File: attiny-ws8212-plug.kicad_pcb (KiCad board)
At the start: 2 copper layers, 25.4 x 22.9 mm, 5 parts, among them J1 USB_A, J2 WS2812, J3 WS2812, J4 WS2812, U1 ATtiny13-20PU

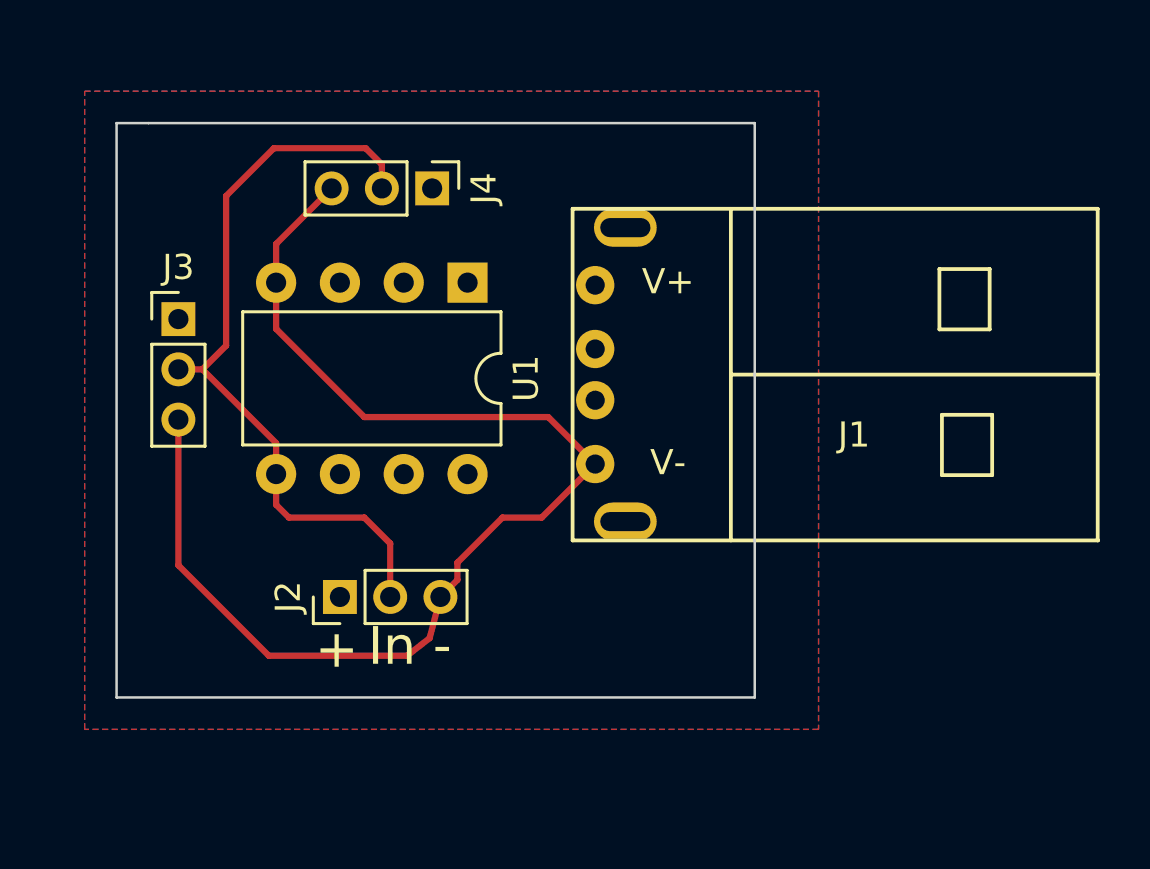
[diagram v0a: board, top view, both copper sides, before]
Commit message: Update schematics to 2.54mm of the pins
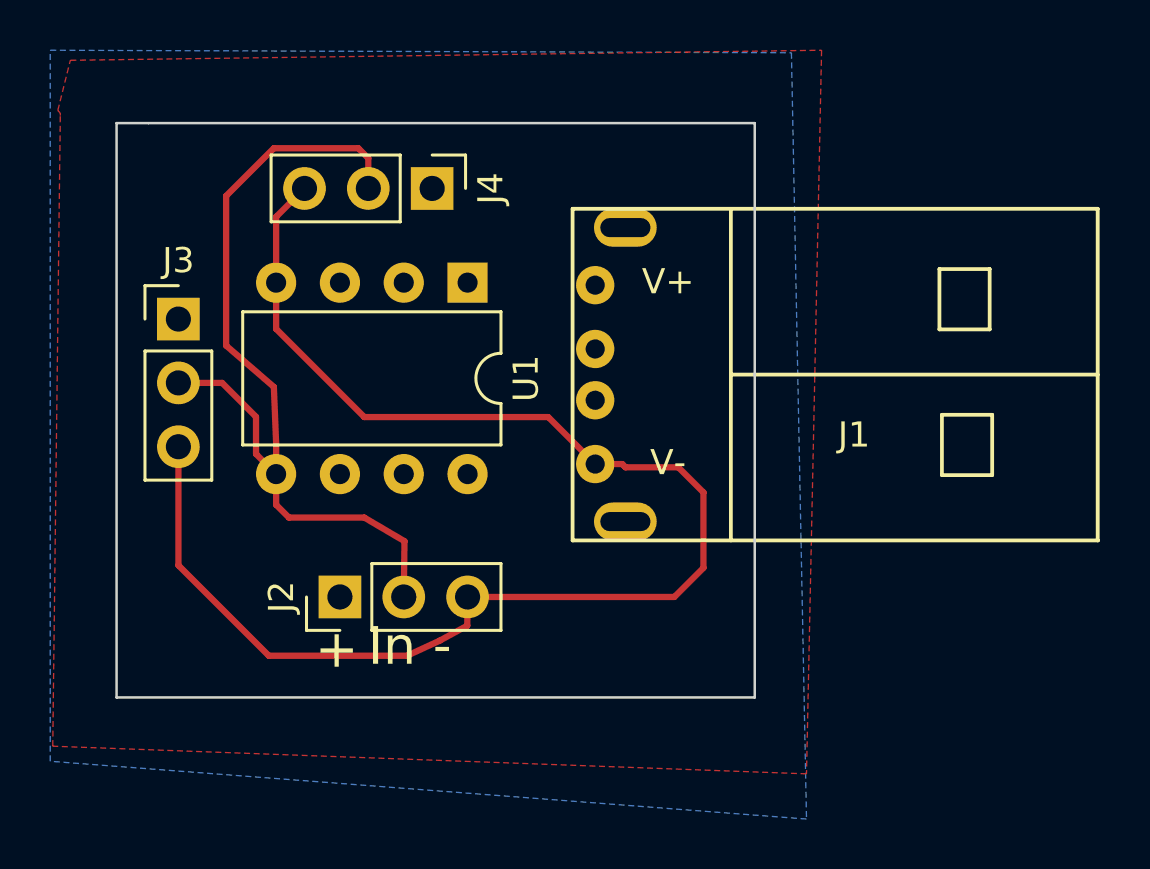
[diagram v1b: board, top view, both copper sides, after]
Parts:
- J2, J3, J4: footprint Connector_PinHeader_2.00mm:PinHeader_1x03_P2.00mm_Vertical -> Connector_PinHeader_2.54mm:PinHeader_1x03_P2.54mm_Vertical
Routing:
- net GND: track 49.4 -> 57.8 mm
- net DataIn: track 30.4 -> 35.6 mm
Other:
- board text added: "Alejandro Gallo 2020"
- board text removed: "Copyright (c) 2019 Alejandro Gallo"
